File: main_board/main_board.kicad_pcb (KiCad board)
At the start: 2 copper layers, 20.3 x 15.2 mm, 20 parts, among them U1 STM32G031G8Ux, U2 AMS1117-3.3

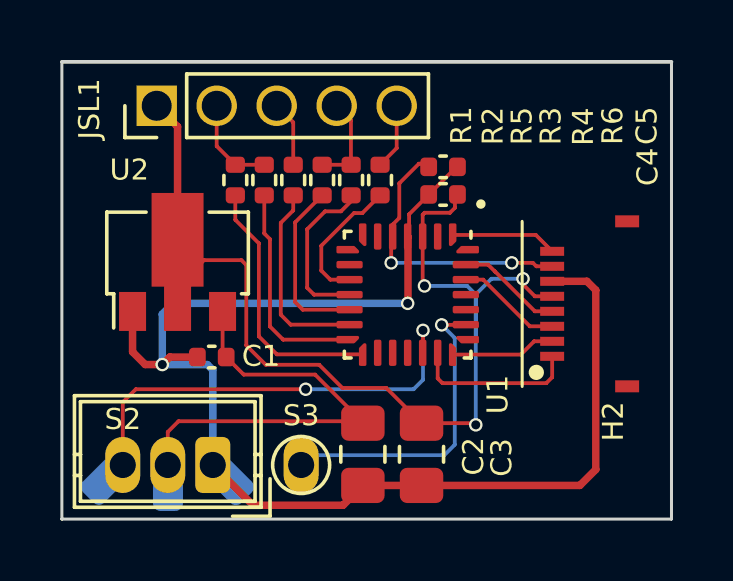
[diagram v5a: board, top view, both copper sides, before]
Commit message: feat(main_board/led): add MOSFET for led bar
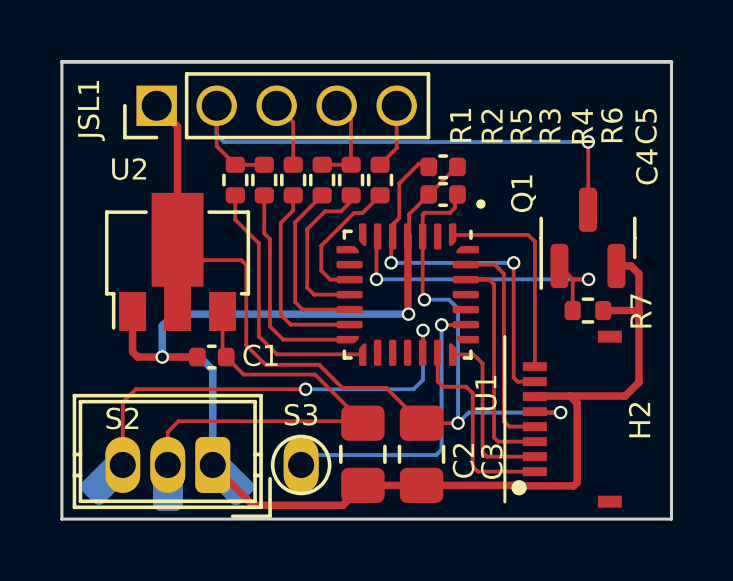
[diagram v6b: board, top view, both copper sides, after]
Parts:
- added Q1: NMOS, Package_TO_SOT_SMD:SOT-23, F.Cu at (104.1, 92.3)
- added R7: 100, Resistor_SMD:R_0402_1005Metric, F.Cu at (104.1, 94.7)
- R1: value 100 -> 680
- R2, R4, R6: value 100 -> 0
- R3: value 100 -> 220
- moved H2 3.89 mm to (103.3, 98.3)
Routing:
- net /LED_HEAD: track 3.19 -> 18.9 mm, vias 0 -> 1
- net /SW: track 0.00 -> 10.8 mm, vias 0 -> 2
- net /UART_TX: track 3.52 -> 7.53 mm
- net /UART_RX: track 3.52 -> 7.45 mm
- net GND: track 45.0 -> 48.6 mm
- net /TP1: track 3.57 -> 7.00 mm
- net /RST: track 9.34 -> 12.6 mm
- net /SWCLK: track 3.50 -> 5.88 mm
- net /VCC: track 36.8 -> 35.2 mm
- net /SWDIO: track 5.51 -> 6.87 mm
- net /SG_BT: track 10.4 -> 9.86 mm

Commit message: feat: modify logo
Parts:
- renumbered JSL1 to JSKX
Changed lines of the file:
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@@
 (kicad_pcb (version 20221018) (generator pcbnew)
   (general
-    (thickness 1.6)
+    (thickness 1)
   )
   (paper "A4")
@@
       (layer "F.SilkS" (type "Top Silk Screen"))
       (layer "F.Paste" (type "Top Solder Paste"))
-      (layer "F.Mask" (type "Top Solder Mask") (thickness 0.01))
+      (layer "F.Mask" (type "Top Solder Mask") (color "Black") (thickness 0.01))
       (layer "F.Cu" (type "copper") (thickness 0.035))
-      (layer "dielectric 1" (type "core") (thickness 1.51) (material "FR4") (epsilon_r 4.5) (loss_tangent 0.02))
+      (layer "dielectric 1" (type "core") (thickness 0.91) (material "FR4") (epsilon_r 4.5) (loss_tangent 0.02))
       (layer "B.Cu" (type "copper") (thickness 0.035))
-      (layer "B.Mask" (type "Bottom Solder Mask") (thickness 0.01))
+      (layer "B.Mask" (type "Bottom Solder Mask") (color "Black") (thickness 0.01))
       (layer "B.Paste" (type "Bottom Solder Paste"))
       (layer "B.SilkS" (type "Bottom Silk Screen"))
@@
     (property "ki_keywords" "connector")
     (attr through_hole)
-    (fp_text reference "JSL1" (at -0.1067 -2.2432 90) (layer "F.SilkS")
-        (effects (font (size 0.7 0.7) (thickness 0.15)))
-    )
+    (fp_text reference "JSKX" (at -0.1067 -2.2432 90) (layer "F.SilkS")
+        (effects (font (size 0.7 0.7) (thickness 0.15)))
+    )
